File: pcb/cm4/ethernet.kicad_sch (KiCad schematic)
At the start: 6 parts, among them J401 HR911130A, U401 TPD4EUSB30, U402 TPD4EUSB30

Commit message: update pcb
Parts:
- C301: renamed from C401; footprint (none) -> Capacitor_SMD:C_0805_2012Metric
- J301: renamed from J401; footprint Connector_RJ:RJ45_Pulse_JK0654219NL_Horizontal -> DF40C-100DS-0.4V_51_:HANRUN_HR911130A; Availability In Stock -> (none); Check_prices https://www.snapeda.com/parts/HR911130A/HanRun/view-part/?r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 -> (none); LCSC (none) -> C54408; MANUFACTURER HanRun -> (none); MAXIMUM_PACKAGE_HEIGHT 13.75 mm -> (none); MF hanrun -> (none); MP HR911130A -> (none); PARTREV A -> (none); Package None -> (none); Price None -> (none); STANDARD Manufacturer Recommendations -> (none); SnapEDA_Link https://www.snapeda.com/parts/HR911130A/HanRun/view-part/?r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 -> (none)
- R301: renamed from R401; footprint (none) -> Resistor_SMD:R_0805_2012Metric
- R302: renamed from R402; footprint (none) -> Resistor_SMD:R_0805_2012Metric
- renumbered U401 to U301, U402 to U302
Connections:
- net TRD0+: now also U302.1 (D1+), U302.10 (NC); no longer U302.4 (D2+), U302.7 (NC)
- net TRD0-: now also U302.2 (D1-), U302.9 (NC); no longer U302.5 (D2-), U302.6 (NC)
- net TRD1+: now also U302.4 (D2+), U302.7 (NC); no longer U302.1 (D1+), U302.10 (NC)
- net TRD1-: now also U301.2 (D1-), U301.9 (NC); no longer U302.2 (D1-), U302.9 (NC)
- net TRD2+: now also U302.5 (D2-), U302.6 (NC); no longer U301.1 (D1+), U301.10 (NC)
- net TRD2-: now also U301.1 (D1+), U301.10 (NC); no longer U301.2 (D1-), U301.9 (NC)

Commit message: update cm4 board
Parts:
- U301, U302: LCSC (none) -> C90627
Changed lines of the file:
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@@
+			)
+		)
+		(property "LCSC" "C90627"
+			(at 186.69 104.14 0)
+			(effects
+				(font
+					(size 1.27 1.27)
+				)
+				(hide yes)
 			)
 		)
@@
 			)
 		)
+		(property "LCSC" "C90627"
+			(at 186.69 63.5 0)
+			(effects
+				(font
+					(size 1.27 1.27)
+				)
+				(hide yes)
+			)
+		)
 		(pin "10"
 		)
@@
 			)
 		)
-		(property "Description" ""
+		(property "Description" "RJ45 Connector"
 			(at 119.38 83.82 0)
 			(effects

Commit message: cm4: update footprint library, add 3d files, update dimensions
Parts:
- J301: footprint DF40C-100DS-0.4V_51_:HANRUN_HR911130A -> PRJ:HANRUN_HR911130A
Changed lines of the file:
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@@
 		(shape input)
 		(at 96.52 76.2 180)
-		(fields_autoplaced yes)
 		(effects
 			(font
@@
 		(shape input)
 		(at 171.45 96.52 180)
-		(fields_autoplaced yes)
 		(effects
 			(font
@@
 		(shape input)
 		(at 203.2 55.88 0)
-		(fields_autoplaced yes)
 		(effects
 			(font
@@
 		(shape input)
 		(at 171.45 101.6 180)
-		(fields_autoplaced yes)
 		(effects
 			(font
@@
 		(shape input)
 		(at 171.45 106.68 180)
-		(fields_autoplaced yes)
 		(effects
 			(font
@@
 		(shape input)
 		(at 171.45 55.88 180)
-		(fields_autoplaced yes)
 		(effects
 			(font
@@
 		(shape input)
 		(at 203.2 96.52 0)
-		(fields_autoplaced yes)
 		(effects
 			(font
@@
 		(shape input)
 		(at 203.2 101.6 0)
-		(fields_autoplaced yes)
 		(effects
 			(font
@@
 		(shape input)
 		(at 203.2 106.68 0)
-		(fields_autoplaced yes)
 		(effects
 			(font
@@
 		(shape input)
 		(at 96.52 60.96 180)
-		(fields_autoplaced yes)
 		(effects
 			(font
@@
 		(shape input)
 		(at 96.52 66.04 180)
-		(fields_autoplaced yes)
 		(effects
 			(font
@@
 		(shape input)
 		(at 171.45 60.96 180)
-		(fields_autoplaced yes)
 		(effects
 			(font
@@
 		(shape input)
 		(at 171.45 71.12 180)
-		(fields_autoplaced yes)
 		(effects
 			(font
@@
 		(shape input)
 		(at 171.45 66.04 180)
-		(fields_autoplaced yes)
 		(effects
 			(font
@@
 		(shape input)
 		(at 96.52 73.66 180)
-		(fields_autoplaced yes)
 		(effects
 			(font
@@
 		(shape input)
 		(at 96.52 63.5 180)
-		(fields_autoplaced yes)
 		(effects
 			(font
@@
 		(shape input)
 		(at 203.2 111.76 0)
-		(fields_autoplaced yes)
 		(effects
 			(font
@@
 		(shape input)
 		(at 96.52 78.74 180)
-		(fields_autoplaced yes)
 		(effects
 			(font
@@
 		(shape input)
 		(at 96.52 71.12 180)
-		(fields_autoplaced yes)
 		(effects
 			(font
@@
 		(shape input)
 		(at 171.45 111.76 180)
-		(fields_autoplaced yes)
 		(effects
 			(font
@@
 		(shape input)
 		(at 96.52 68.58 180)
-		(fields_autoplaced yes)
 		(effects
 			(font
@@
 		(shape input)
 		(at 203.2 66.04 0)
-		(fields_autoplaced yes)
 		(effects
 			(font
@@
 		(shape input)
 		(at 86.36 93.98 180)
-		(fields_autoplaced yes)
 		(effects
 			(font
@@
 		(shape input)
 		(at 203.2 71.12 0)
-		(fields_autoplaced yes)
 		(effects
 			(font
@@
 		(shape input)
 		(at 203.2 60.96 0)
-		(fields_autoplaced yes)
 		(effects
 			(font
@@
 		(shape input)
 		(at 86.36 106.68 180)
-		(fields_autoplaced yes)
 		(effects
 			(font
@@
 			)
 		)
-		(property "Footprint" "DF40C-100DS-0.4V_51_:HANRUN_HR911130A"
+		(property "Footprint" "PRJ:HANRUN_HR911130A"
 			(at 119.38 83.82 0)
 			(effects

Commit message: update lscs fields
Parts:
- C301: LCSC (none) -> C49678
- R301, R302: LCSC (none) -> C17710
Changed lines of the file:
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@@
 			)
 		)
-		(property "LCSC" ""
+		(property "LCSC" "C49678"
 			(at 99.06 53.34 0)
 			(effects
@@
 			)
 		)
-		(property "LCSC" ""
+		(property "LCSC" "C17710"
 			(at 92.71 106.68 0)
 			(effects
@@
 			)
 		)
-		(property "LCSC" ""
+		(property "LCSC" "C17710"
 			(at 92.71 93.98 0)
 			(effects

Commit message: upgrade to kicad 9.0.0
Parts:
- J301: Availability (none) -> In Stock; Check_prices (none) -> https://www.snapeda.com/parts/HR911130A/HanRun/view-part/?r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; MANUFACTURER (none) -> HanRun; MAXIMUM_PACKAGE_HEIGHT (none) -> 13.75 mm; MF (none) -> hanrun; MP (none) -> HR911130A; PARTREV (none) -> A; Package (none) -> None; Price (none) -> None; STANDARD (none) -> Manufacturer Recommendations; SnapEDA_Link (none) -> https://www.snapeda.com/parts/HR911130A/HanRun/view-part/?r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

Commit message: update cm4 board
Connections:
- net ETH_GREEN renamed ETH_LED_G
- net ETH_YELLOW renamed ETH_LED_Y
- net TRD0+ renamed ETH_TRD0_P
- net TRD0- renamed ETH_TRD0_M
- net TRD1+ renamed ETH_TRD1_P
- net TRD1- renamed ETH_TRD1_M
- net TRD2+ renamed ETH_TRD2_P
- net TRD2- renamed ETH_TRD2_M
- net TRD3+ renamed ETH_TRD3_P
- net TRD3- renamed ETH_TRD3_M
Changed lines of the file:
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@@
 		)
 	)
-	(hierarchical_label "TRD3+"
+	(hierarchical_label "ETH_TRD3_P"
 		(shape input)
 		(at 96.52 76.2 180)
@@
 		)
 	)
-	(hierarchical_label "TRD0+"
+	(hierarchical_label "ETH_TRD0_P"
 		(shape input)
 		(at 171.45 96.52 180)
@@
 		)
 	)
-	(hierarchical_label "TRD3+"
+	(hierarchical_label "ETH_TRD3_P"
 		(shape input)
 		(at 203.2 55.88 0)
@@
 		)
 	)
-	(hierarchical_label "TRD0+"
+	(hierarchical_label "ETH_TRD0_P"
 		(shape input)
 		(at 171.45 101.6 180)
@@
 		)
 	)
-	(hierarchical_label "TRD0-"
+	(hierarchical_label "ETH_TRD0_M"
 		(shape input)
 		(at 171.45 106.68 180)
@@
 		)
 	)
-	(hierarchical_label "TRD2-"
+	(hierarchical_label "ETH_TRD2_M"
 		(shape input)
 		(at 171.45 55.88 180)
@@
 		)
 	)
-	(hierarchical_label "TRD1+"
+	(hierarchical_label "ETH_TRD1_P"
 		(shape input)
 		(at 203.2 96.52 0)
@@
 		)
 	)
-	(hierarchical_label "TRD1+"
+	(hierarchical_label "ETH_TRD1_P"
 		(shape input)
 		(at 203.2 101.6 0)
@@
 		)
 	)
-	(hierarchical_label "TRD2+"
+	(hierarchical_label "ETH_TRD2_P"
 		(shape input)
 		(at 203.2 106.68 0)
@@
 		)
 	)
-	(hierarchical_label "TRD0+"
+	(hierarchical_label "ETH_TRD0_P"
 		(shape input)
 		(at 96.52 60.96 180)
@@
 		)
 	)
-	(hierarchical_label "TRD1+"
+	(hierarchical_label "ETH_TRD1_P"
 		(shape input)
 		(at 96.52 66.04 180)
@@
 		)
 	)
-	(hierarchical_label "TRD2-"
+	(hierarchical_label "ETH_TRD2_M"
 		(shape input)
 		(at 171.45 60.96 180)
@@
 		)
 	)
-	(hierarchical_label "TRD1-"
+	(hierarchical_label "ETH_TRD1_M"
 		(shape input)
 		(at 171.45 71.12 180)
@@
 		)
 	)
-	(hierarchical_label "TRD1-"
+	(hierarchical_label "ETH_TRD1_M"
 		(shape input)
 		(at 171.45 66.04 180)
@@
 		)
 	)
-	(hierarchical_label "TRD1-"
+	(hierarchical_label "ETH_TRD1_M"
 		(shape input)
 		(at 96.52 73.66 180)
@@
 		)
 	)
-	(hierarchical_label "TRD0-"
+	(hierarchical_label "ETH_TRD0_M"
 		(shape input)
 		(at 96.52 63.5 180)
@@
 		)
 	)
-	(hierarchical_label "TRD2+"
+	(hierarchical_label "ETH_TRD2_P"
 		(shape input)
 		(at 203.2 111.76 0)
@@
 		)
 	)
-	(hierarchical_label "TRD3-"
+	(hierarchical_label "ETH_TRD3_M"
 		(shape input)
 		(at 96.52 78.74 180)
@@
 		)
 	)
-	(hierarchical_label "TRD2-"
+	(hierarchical_label "ETH_TRD2_M"
 		(shape input)
 		(at 96.52 71.12 180)
@@
 		)
 	)
-	(hierarchical_label "TRD0-"
+	(hierarchical_label "ETH_TRD0_M"
 		(shape input)
 		(at 171.45 111.76 180)
@@
 		)
 	)
-	(hierarchical_label "TRD2+"
+	(hierarchical_label "ETH_TRD2_P"
 		(shape input)
 		(at 96.52 68.58 180)
@@
 		)
 	)
-	(hierarchical_label "TRD3-"
+	(hierarchical_label "ETH_TRD3_M"
 		(shape input)
 		(at 203.2 66.04 0)
@@
 		)
 	)
-	(hierarchical_label "ETH_GREEN"
+	(hierarchical_label "ETH_LED_G"
 		(shape input)
 		(at 86.36 93.98 180)
@@
 		)
 	)
-	(hierarchical_label "TRD3-"
+	(hierarchical_label "ETH_TRD3_M"
 		(shape input)
 		(at 203.2 71.12 0)
@@
 		)
 	)
-	(hierarchical_label "TRD3+"
+	(hierarchical_label "ETH_TRD3_P"
 		(shape input)
 		(at 203.2 60.96 0)
@@
 		)
 	)
-	(hierarchical_label "ETH_YELLOW"
+	(hierarchical_label "ETH_LED_Y"
 		(shape input)
 		(at 86.36 106.68 180)

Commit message: update ALL parts
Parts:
- C301: LCSC C49678 -> C28233
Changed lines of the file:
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@@
+			)
+		)
+		(property "MOUSER" ""
+			(at 186.69 104.14 0)
+			(effects
+				(font
+					(size 1.27 1.27)
+				)
 			)
 		)
@@
 			)
 		)
+		(property "MOUSER" ""
+			(at 186.69 63.5 0)
+			(effects
+				(font
+					(size 1.27 1.27)
+				)
+			)
+		)
 		(pin "10"
 		)
@@
 			)
 		)
-		(property "LCSC" "C49678"
+		(property "LCSC" "C28233"
 			(at 99.06 53.34 0)
 			(effects
@@
 				)
 				(hide yes)
+			)
+		)
+		(property "MOUSER" ""
+			(at 99.06 53.34 0)
+			(effects
+				(font
+					(size 1.27 1.27)
+				)
 			)
 		)
@@
 			)
 		)
+		(property "MOUSER" ""
+			(at 92.71 106.68 0)
+			(effects
+				(font
+					(size 1.27 1.27)
+				)
+			)
+		)
 		(pin "1"
 		)
@@
 			)
 		)
+		(property "MOUSER" ""
+			(at 119.38 83.82 0)
+			(effects
+				(font
+					(size 1.27 1.27)
+				)
+			)
+		)
 		(pin "10"
 		)
@@
 			)
 		)
+		(property "MOUSER" ""
+			(at 92.71 93.98 0)
+			(effects
+				(font
+					(size 1.27 1.27)
+				)
+			)
+		)

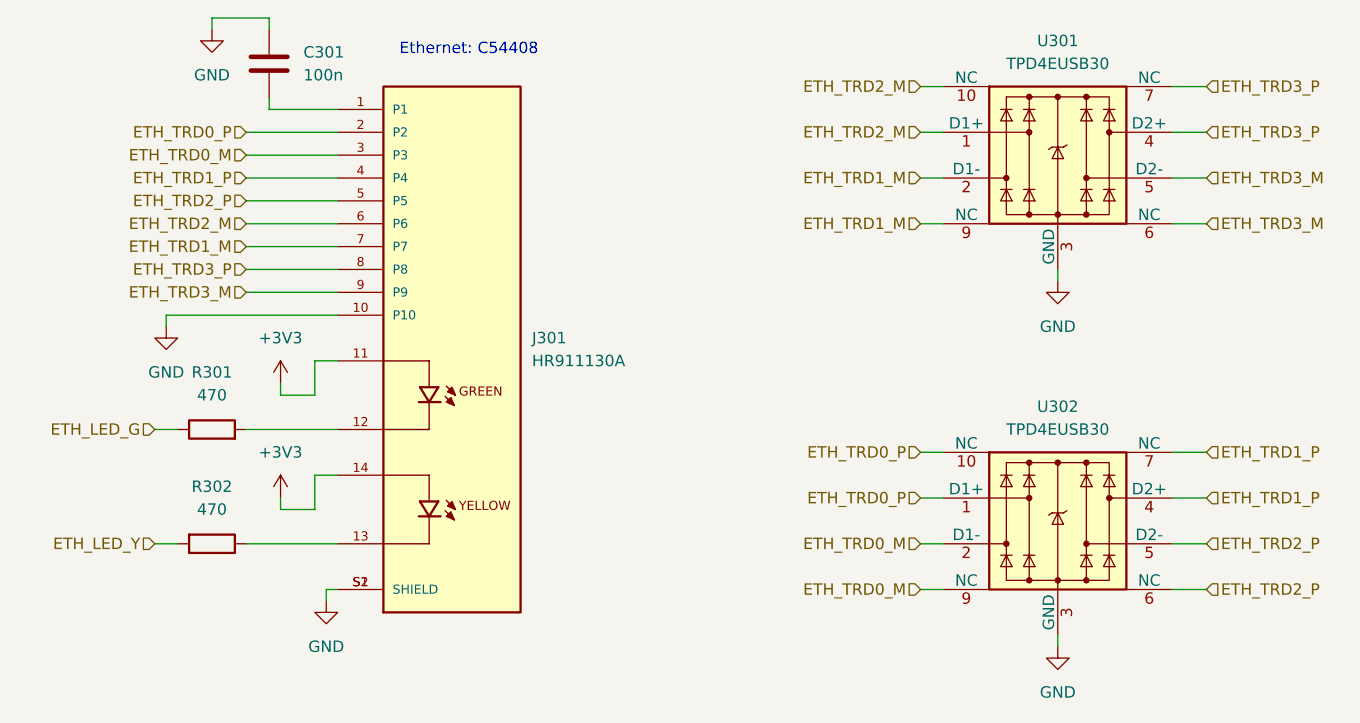
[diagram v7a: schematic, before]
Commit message: rename differential nets correctly and fix cm4 footprint
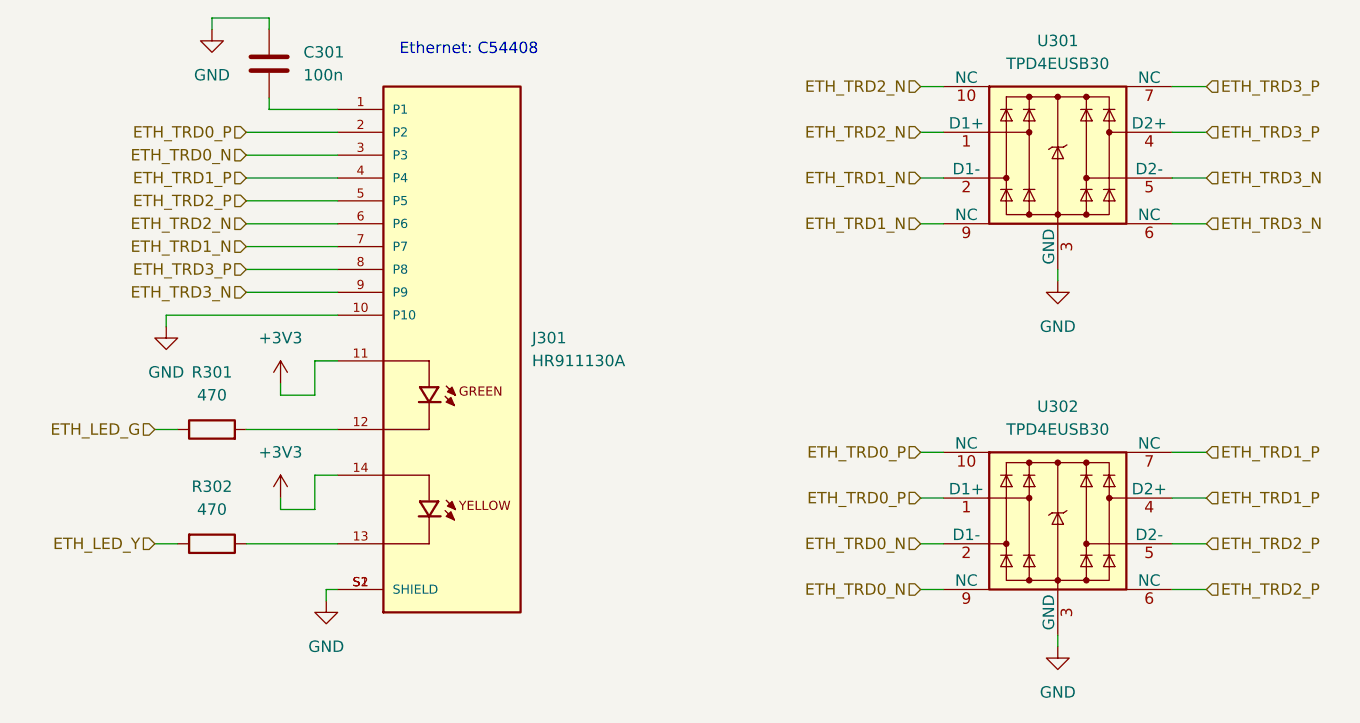
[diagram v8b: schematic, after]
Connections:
- net ETH_TRD0_M renamed ETH_TRD0_N
- net ETH_TRD1_M renamed ETH_TRD1_N
- net ETH_TRD2_M renamed ETH_TRD2_N
- net ETH_TRD3_M renamed ETH_TRD3_N
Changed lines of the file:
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@@
 		)
 	)
-	(hierarchical_label "ETH_TRD0_M"
+	(hierarchical_label "ETH_TRD0_N"
 		(shape input)
 		(at 171.45 106.68 180)
@@
 		)
 	)
-	(hierarchical_label "ETH_TRD2_M"
+	(hierarchical_label "ETH_TRD2_N"
 		(shape input)
 		(at 171.45 55.88 180)
@@
 		)
 	)
-	(hierarchical_label "ETH_TRD2_M"
+	(hierarchical_label "ETH_TRD2_N"
 		(shape input)
 		(at 171.45 60.96 180)
@@
 		)
 	)
-	(hierarchical_label "ETH_TRD1_M"
+	(hierarchical_label "ETH_TRD1_N"
 		(shape input)
 		(at 171.45 71.12 180)
@@
 		)
 	)
-	(hierarchical_label "ETH_TRD1_M"
+	(hierarchical_label "ETH_TRD1_N"
 		(shape input)
 		(at 171.45 66.04 180)
@@
 		)
 	)
-	(hierarchical_label "ETH_TRD1_M"
+	(hierarchical_label "ETH_TRD1_N"
 		(shape input)
 		(at 96.52 73.66 180)
@@
 		)
 	)
-	(hierarchical_label "ETH_TRD0_M"
+	(hierarchical_label "ETH_TRD0_N"
 		(shape input)
 		(at 96.52 63.5 180)
@@
 		)
 	)
-	(hierarchical_label "ETH_TRD3_M"
+	(hierarchical_label "ETH_TRD3_N"
 		(shape input)
 		(at 96.52 78.74 180)
@@
 		)
 	)
-	(hierarchical_label "ETH_TRD2_M"
+	(hierarchical_label "ETH_TRD2_N"
 		(shape input)
 		(at 96.52 71.12 180)
@@
 		)
 	)
-	(hierarchical_label "ETH_TRD0_M"
+	(hierarchical_label "ETH_TRD0_N"
 		(shape input)
 		(at 171.45 111.76 180)
@@
 		)
 	)
-	(hierarchical_label "ETH_TRD3_M"
+	(hierarchical_label "ETH_TRD3_N"
 		(shape input)
 		(at 203.2 66.04 0)
@@
 		)
 	)
-	(hierarchical_label "ETH_TRD3_M"
+	(hierarchical_label "ETH_TRD3_N"
 		(shape input)
 		(at 203.2 71.12 0)
